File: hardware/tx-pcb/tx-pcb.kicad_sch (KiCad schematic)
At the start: 51 parts, among them J1 Conn_01x07, J2 Conn_To_J2, J3 BLIO, J4 Conn_01x05, J5 Conn_01x04, J7 Conn_01x02_Pin, SW1 BOOT0, SW2 RESET, SW3 BTN1, SW4 BTN2, SW5 BTN3, SW6 BTN4, SW7 BTN5, SW9 SW_SPDT, U2 STM32WB55CEUx, X1 Q22FA12800025, X2 ABS07-32.768KHZ-1-T

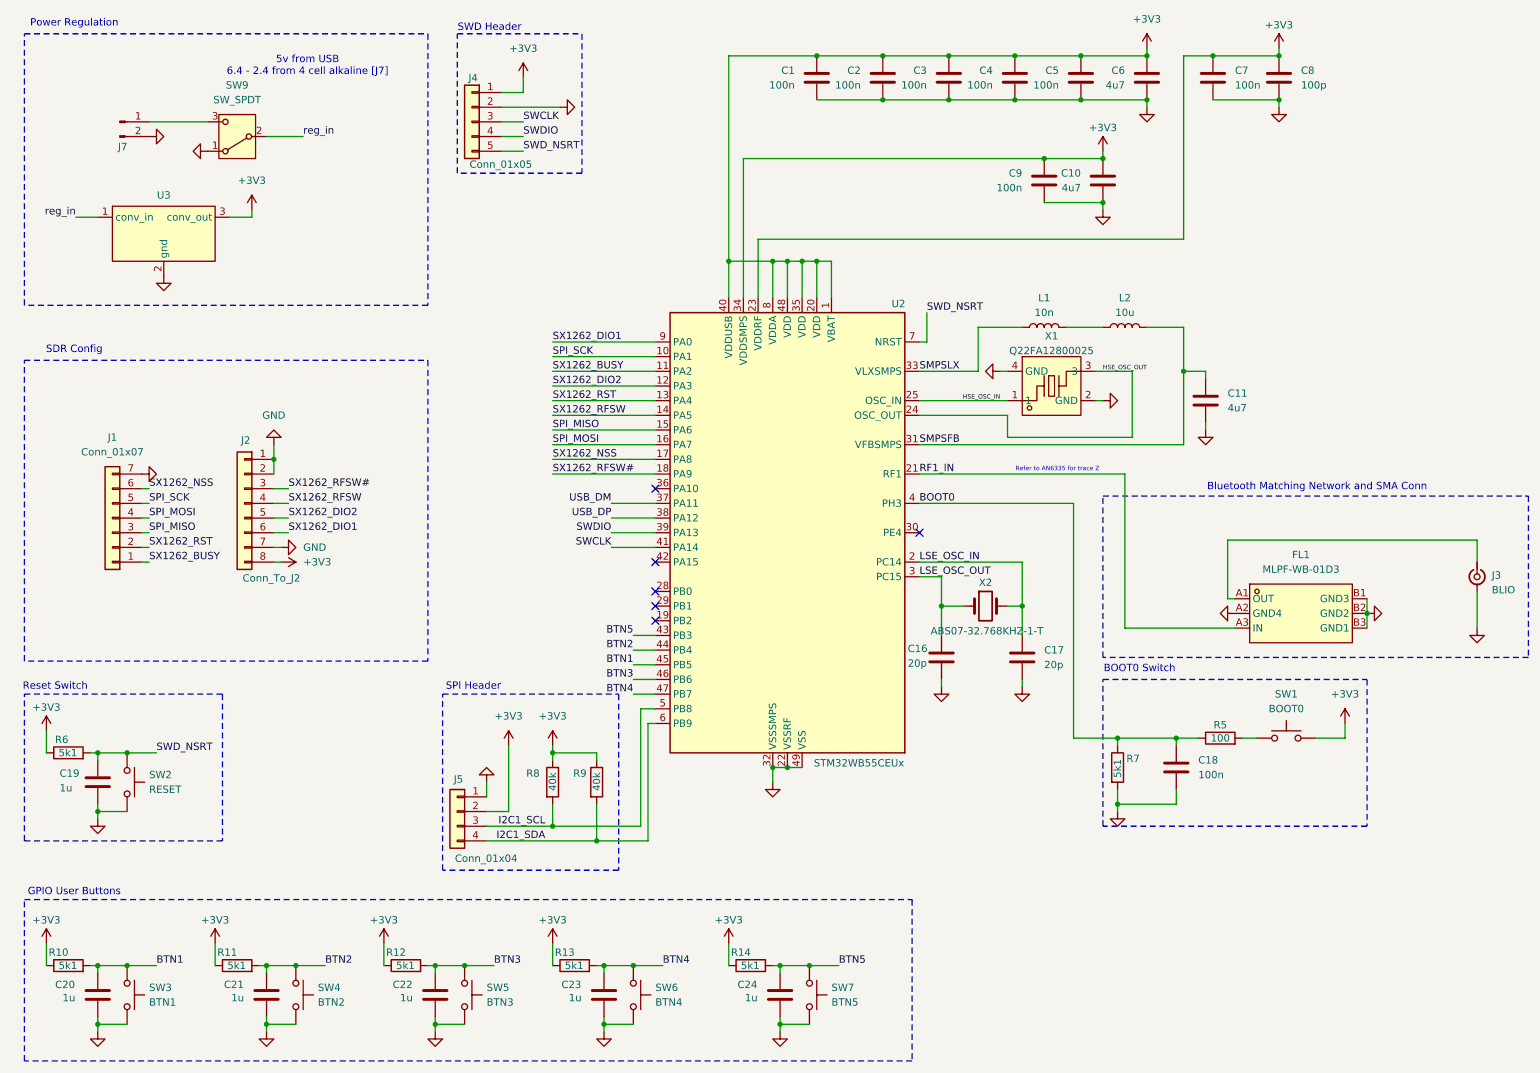
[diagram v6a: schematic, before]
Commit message: added UART to PCB, cleaned up wiring
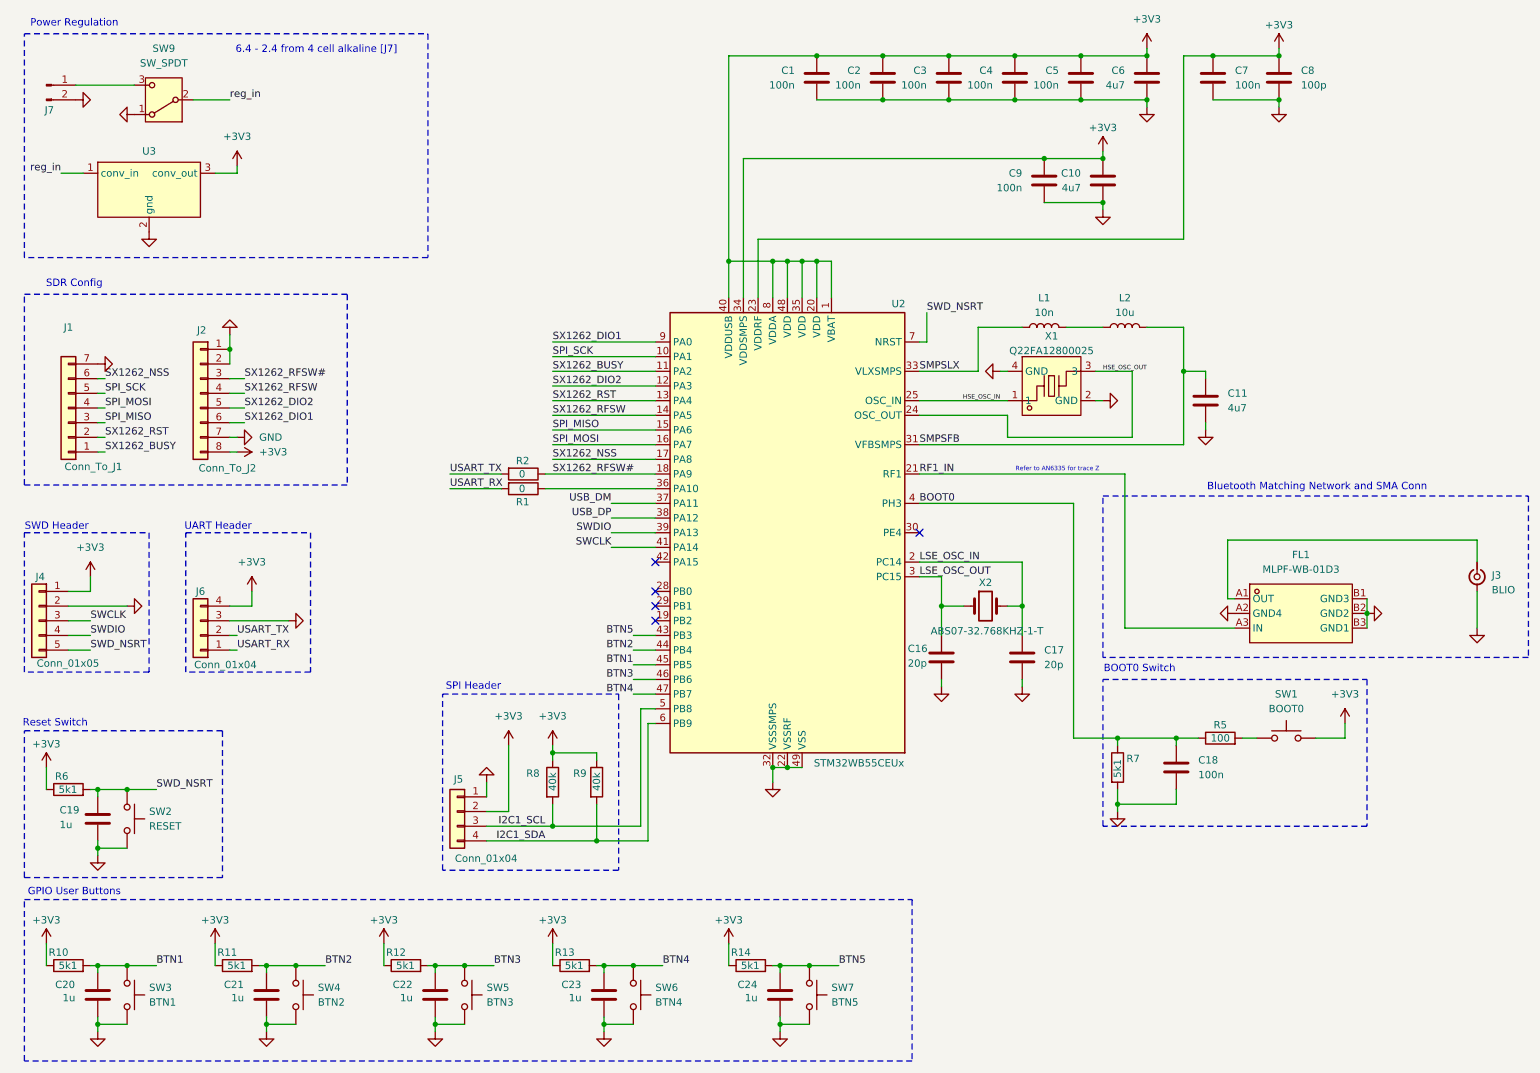
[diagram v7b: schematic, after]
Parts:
- added J6: Conn_01x04, Connector_PinHeader_2.54mm:PinHeader_1x04_P2.54mm_Vertical, symbol Connector_Generic:Conn_01x04
- added R1, R2: 0, Resistor_SMD:R_0805_2012Metric_Pad1.20x1.40mm_HandSolder, symbol Device:R
- J1: value Conn_01x07 -> Conn_To_J1
- J3: footprint SMA_Samtec_SMA-J-P-H-ST-EM1_EdgeMount -> Connector_Coaxial:SMA_Samtec_SMA-J-P-H-ST-EM1_EdgeMount
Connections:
- net +3V3: now also J6.4 (Pin_4)
- net GND: now also J6.3 (Pin_3)
- net SX1262_RFSW#: now also R2.1
- net at U2.36 (PA10): now also R1.1
- new net USART_RX: J6.1 (Pin_1), R1.2
- new net USART_TX: J6.2 (Pin_2), R2.2
- no-connect marks 6 -> 5
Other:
- note added: "6.4 - 2.4 from 4 cell alkaline [J7]"
- note added: "UART Header"
- note removed: "5v from USB 6.4 - 2.4 from 4 cell alkaline [J7]"
- moved on the sheet: C19, J1, J2, J4, J7, R6, SW2, SW9, U3

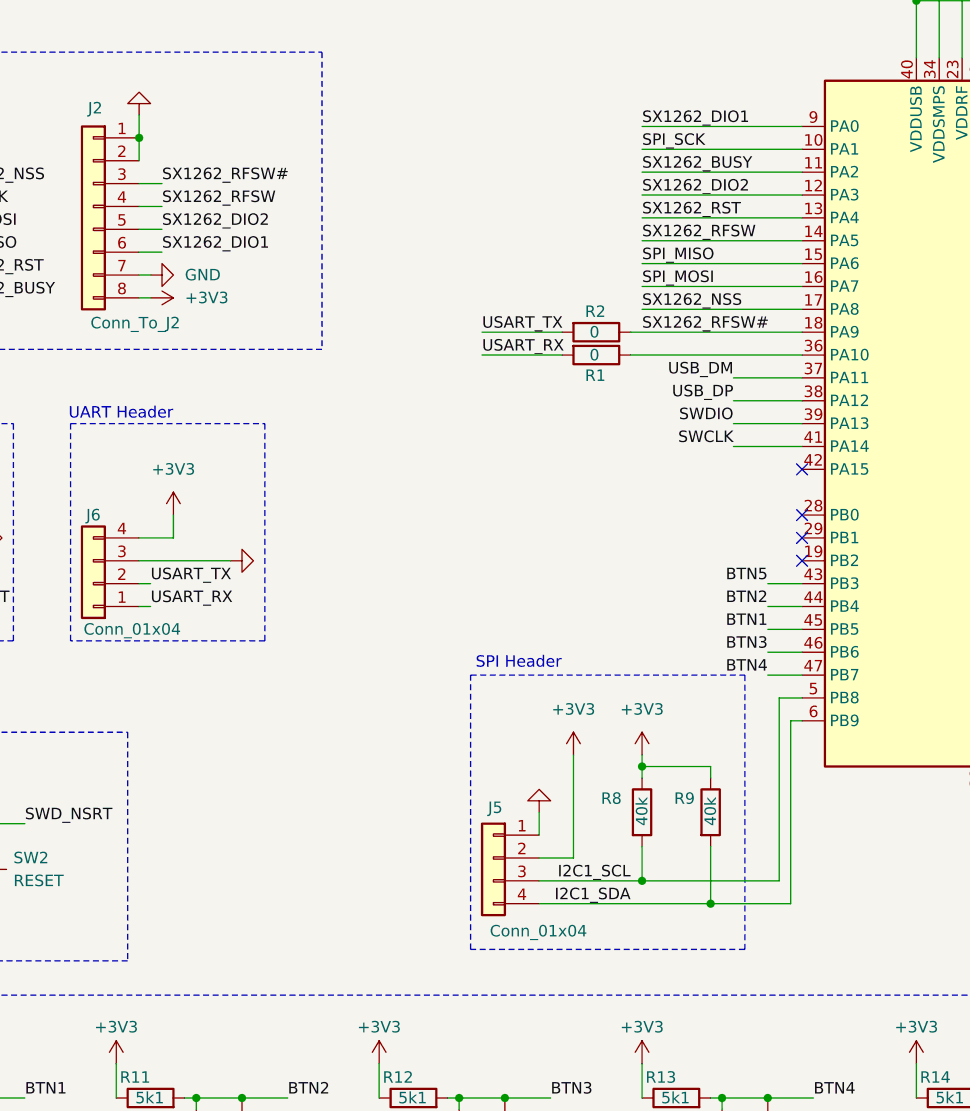
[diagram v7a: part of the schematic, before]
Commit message: fixed the pinouts to properly match WB55CCU6 CubeMX software options
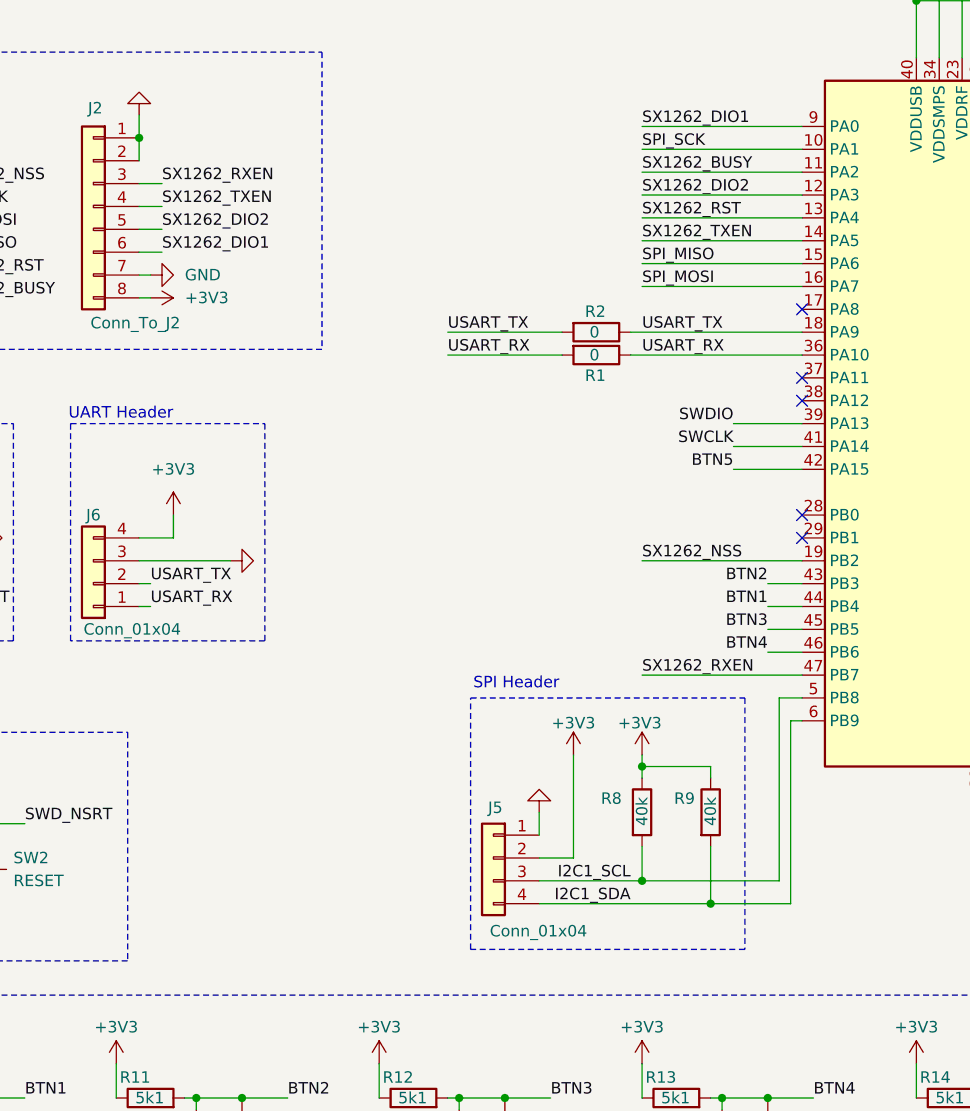
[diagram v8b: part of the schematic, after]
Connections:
- net BTN1: now also U2.44 (PB4); no longer U2.45 (PB5)
- net BTN2: now also U2.43 (PB3); no longer U2.44 (PB4)
- net BTN3: now also U2.45 (PB5); no longer U2.46 (PB6)
- net BTN4: now also U2.46 (PB6); no longer U2.47 (PB7)
- net BTN5: now also U2.42 (PA15); no longer U2.43 (PB3)
- net SX1262_NSS: now also U2.19 (PB2); no longer U2.17 (PA8)
- net USART_RX: now also R1.1, U2.36 (PA10)
- net USART_TX: now also R2.1, U2.18 (PA9)
- net SX1262_RFSW renamed SX1262_TXEN
- removed net SX1262_RFSW#: J2.3 (Pin_3), R2.1, U2.18 (PA9)
- net USB_DM: no longer names the net of U2.37 (PA11)
- net USB_DP: no longer names the net of U2.38 (PA12)
- new net SX1262_RXEN: J2.3 (Pin_3), U2.47 (PB7)
- no-connect marks 5 -> 6
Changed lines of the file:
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@@
 	)
 	(rectangle
-		(start 87.63 133.35)
+		(start 87.63 135.89)
 		(end 118.11 163.83)
 		(stroke
@@
 	(text "SPI Header"
 		(exclude_from_sim no)
-		(at 92.964 132.08 0)
+		(at 92.71 134.366 0)
 		(effects
 			(font
@@
 	)
 	(no_connect
-		(at 124.46 120.65)
+		(at 124.46 100.33)
 	)
 	(no_connect
-		(at 124.46 110.49)
+		(at 124.46 118.11)
 	)
 	(no_connect
-		(at 124.46 118.11)
+		(at 124.46 102.87)
+	)
+	(no_connect
+		(at 124.46 92.71)
 	)
 	(wire
@@
 	(wire
 		(pts
+			(xy 116.84 110.49) (xy 124.46 110.49)
+		)
+		(stroke
+			(width 0)
+			(type default)
+		)
+	)
+	(wire
+		(pts
 			(xy 198.12 22.86) (xy 186.69 22.86)
 		)
@@
 	(wire
 		(pts
-			(xy 88.9 95.25) (xy 97.79 95.25)
+			(xy 85.09 95.25) (xy 97.79 95.25)
 		)
 		(stroke
@@
 	(wire
 		(pts
-			(xy 116.84 100.33) (xy 124.46 100.33)
-		)
-		(stroke
-			(width 0)
-			(type default)
-		)
-	)
-	(wire
-		(pts
 			(xy 204.47 140.97) (xy 214.63 140.97)
 		)
@@
 	(wire
 		(pts
-			(xy 106.68 92.71) (xy 124.46 92.71)
-		)
-		(stroke
-			(width 0)
-			(type default)
-		)
-	)
-	(wire
-		(pts
 			(xy 266.7 115.57) (xy 266.7 121.92)
 		)
@@
 	(wire
 		(pts
-			(xy 88.9 97.79) (xy 97.79 97.79)
+			(xy 85.09 97.79) (xy 97.79 97.79)
 		)
 		(stroke
@@
 	(wire
 		(pts
+			(xy 106.68 120.65) (xy 124.46 120.65)
+		)
+		(stroke
+			(width 0)
+			(type default)
+		)
+	)
+	(wire
+		(pts
 			(xy 152.4 58.42) (xy 149.86 58.42)
 		)
@@
 	(wire
 		(pts
+			(xy 106.68 133.35) (xy 124.46 133.35)
+		)
+		(stroke
+			(width 0)
+			(type default)
+		)
+	)
+	(wire
+		(pts
 			(xy 26.67 180.34) (xy 27.94 180.34)
 		)
@@
 	(wire
 		(pts
-			(xy 120.65 133.35) (xy 124.46 133.35)
-		)
-		(stroke
-			(width 0)
-			(type default)
-		)
-	)
-	(wire
-		(pts
 			(xy 137.16 58.42) (xy 137.16 64.77)
 		)
@@
 	(wire
 		(pts
-			(xy 116.84 102.87) (xy 124.46 102.87)
-		)
-		(stroke
-			(width 0)
-			(type default)
-		)
-	)
-	(wire
-		(pts
 			(xy 185.42 88.9) (xy 207.01 88.9)
 		)
@@
 	)
 	(label "BTN1"
-		(at 120.65 128.27 180)
+		(at 120.65 125.73 180)
 		(effects
 			(font
@@
 		)
 	)
-	(label "USB_DP"
-		(at 116.84 102.87 180)
-		(effects
-			(font
-				(size 1.27 1.27)
-			)
-			(justify right bottom)
-		)
-	)
 	(label "SPI_MOSI"
 		(at 106.68 90.17 0)
@@
 		)
 	)
+	(label "SX1262_NSS"
+		(at 106.68 120.65 0)
+		(effects
+			(font
+				(size 1.27 1.27)
+			)
+			(justify left bottom)
+		)
+	)
 	(label "SPI_MISO"
 		(at 29.21 86.36 0)
@@
 	)
 	(label "USART_TX"
-		(at 88.9 95.25 0)
+		(at 85.09 95.25 0)
 		(effects
 			(font
@@
 		)
 	)
-	(label "SX1262_NSS"
-		(at 106.68 92.71 0)
+	(label "reg_in"
+		(at 50.8 30.48 0)
 		(effects
 			(font
@@
 		)
 	)
-	(label "BTN3"
-		(at 120.65 130.81 180)
+	(label "SX1262_TXEN"
+		(at 106.68 85.09 0)
 		(effects
 			(font
 				(size 1.27 1.27)
 			)
-			(justify right bottom)
+			(justify left bottom)
 		)
 	)
-	(label "reg_in"
-		(at 50.8 30.48 0)
+	(label "SX1262_RXEN"
+		(at 106.68 133.35 0)
 		(effects
 			(font
@@
 		)
 	)
-	(label "USB_DM"
-		(at 116.84 100.33 180)
+	(label "BTN4"
+		(at 120.65 130.81 180)
 		(effects
 			(font
@@
 		)
 	)
-	(label "SX1262_RFSW"
-		(at 106.68 85.09 0)
+	(label "BTN3"
+		(at 120.65 128.27 180)
 		(effects
 			(font
 				(size 1.27 1.27)
 			)
-			(justify left bottom)
+			(justify right bottom)
 		)
 	)
@@
 		)
 	)
-	(label "BTN5"
-		(at 120.65 123.19 180)
+	(label "RF1_IN"
+		(at 170.18 95.25 0)
 		(effects
 			(font
 				(size 1.27 1.27)
 			)
-			(justify right bottom)
+			(justify left bottom)
 		)
 	)
-	(label "RF1_IN"
-		(at 170.18 95.25 0)
+	(label "SX1262_TXEN"
+		(at 53.34 81.28 0)
 		(effects
 			(font
@@
 		)
 	)
-	(label "SX1262_RFSW"
-		(at 53.34 81.28 0)
+	(label "BTN5"
+		(at 116.84 110.49 180)
+		(effects
+			(font
+				(size 1.27 1.27)
+			)
+			(justify right bottom)
+		)
+	)
+	(label "USART_TX"
+		(at 106.68 95.25 0)
 		(effects
 			(font
@@
 		)
 	)
-	(label "BTN2"
-		(at 120.65 125.73 180)
-		(effects
-			(font
-				(size 1.27 1.27)
-			)
-			(justify right bottom)
-		)
-	)
 	(label "SPI_MOSI"
 		(at 29.21 83.82 0)
@@
 	)
 	(label "USART_RX"
-		(at 88.9 97.79 0)
+		(at 85.09 97.79 0)
+		(effects
+			(font
+				(size 1.27 1.27)
+			)
+			(justify left bottom)
+		)
+	)
+	(label "USART_RX"
+		(at 106.68 97.79 0)
 		(effects
 			(font
@@
 		)
 	)
-	(label "SX1262_RFSW#"
-		(at 106.68 95.25 0)
-		(effects
-			(font
-				(size 1.27 1.27)
-			)
-			(justify left bottom)
-		)
-	)
 	(label "reg_in"
 		(at 21.59 43.18 180)
@@
 		)
 	)
-	(label "SX1262_RFSW#"
+	(label "SX1262_RXEN"
 		(at 53.34 78.74 0)
 		(effects
@@
 		)
 	)
+	(label "BTN2"
+		(at 120.65 123.19 180)
+		(effects
+			(font
+				(size 1.27 1.27)
+			)
+			(justify right bottom)
+		)
+	)
 	(label "SPI_MISO"
 		(at 106.68 87.63 0)
@@
 		)
 	)
-	(label "BTN4"
-		(at 120.65 133.35 180)
-		(effects
-			(font
-				(size 1.27 1.27)
-			)
-			(justify right bottom)
-		)
-	)
 	(label "SX1262_DIO1"
 		(at 106.68 72.39 0)
@@
 		(in_pos_files yes)
 		(dnp no)
-		(fields_autoplaced yes)
 		(property "Reference" "#PWR032"
 			(at 106.68 146.05 0)
@@
 		)
 		(property "Value" "+3V3"
-			(at 106.68 137.16 0)
+			(at 106.426 138.684 0)
 			(show_name no)
 			(do_not_autoplace no)
@@
 		(in_pos_files yes)
 		(dnp no)
-		(fields_autoplaced yes)
 		(property "Reference" "#PWR031"
 			(at 99.06 146.05 0)
@@
 		)
 		(property "Value" "+3V3"
-			(at 99.06 137.16 0)
+			(at 99.06 138.684 0)
 			(show_name no)
 			(do_not_autoplace no)
